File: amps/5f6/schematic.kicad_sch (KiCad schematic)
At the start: 69 parts, among them T3 2R sec

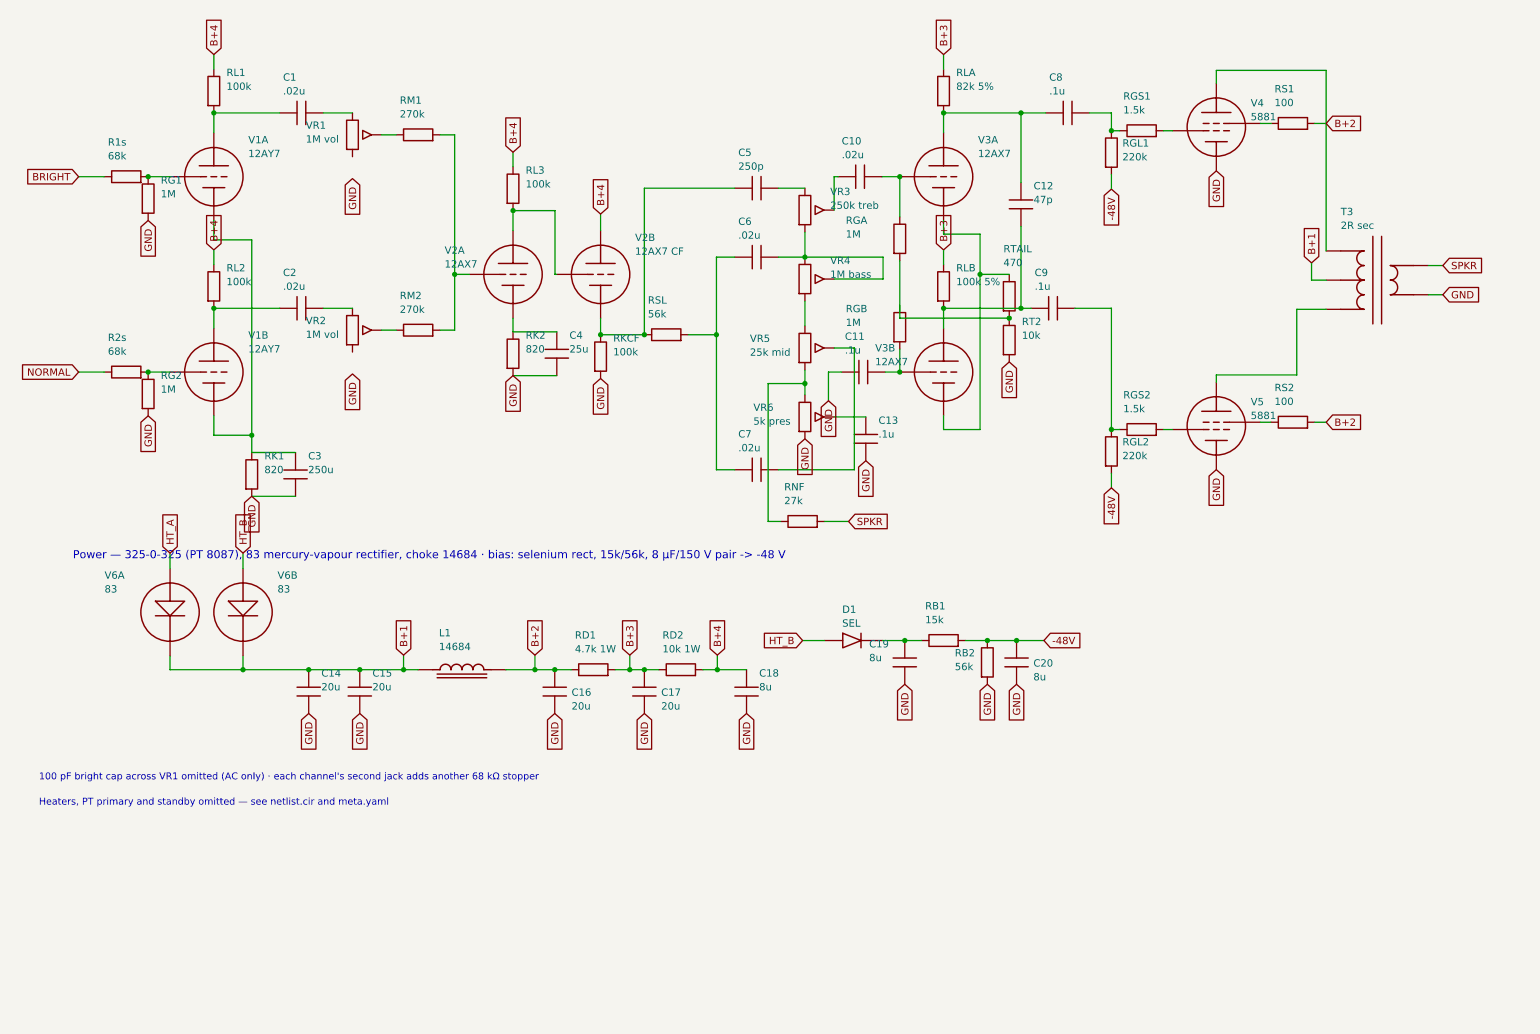
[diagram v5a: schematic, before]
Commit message: Fix: deterministic schematic ids and wires split at every join
- _u() is uuid5 over (amp id, emission order), so a regeneration of an
  unchanged script is byte-identical and a drift gate becomes possible
- write() splits wire segments at symbol pins, wire ends and junction dots,
  so the file connects exactly what the drawing shows under KiCad's
  endpoint-only semantics (270 pins were on a wire's interior; net
  partitions unchanged on all 38 sheets)
- all sheets regenerated; aa864-bassman title block was stale (draft) and
  now matches meta.yaml (verified)

Co-Authored-By: Claude Fable 5.1 <noreply@anthropic.com>
Claude-Session: https://claude.ai/code/session_01KBMfdh37HmCL2iWcBiL5J1
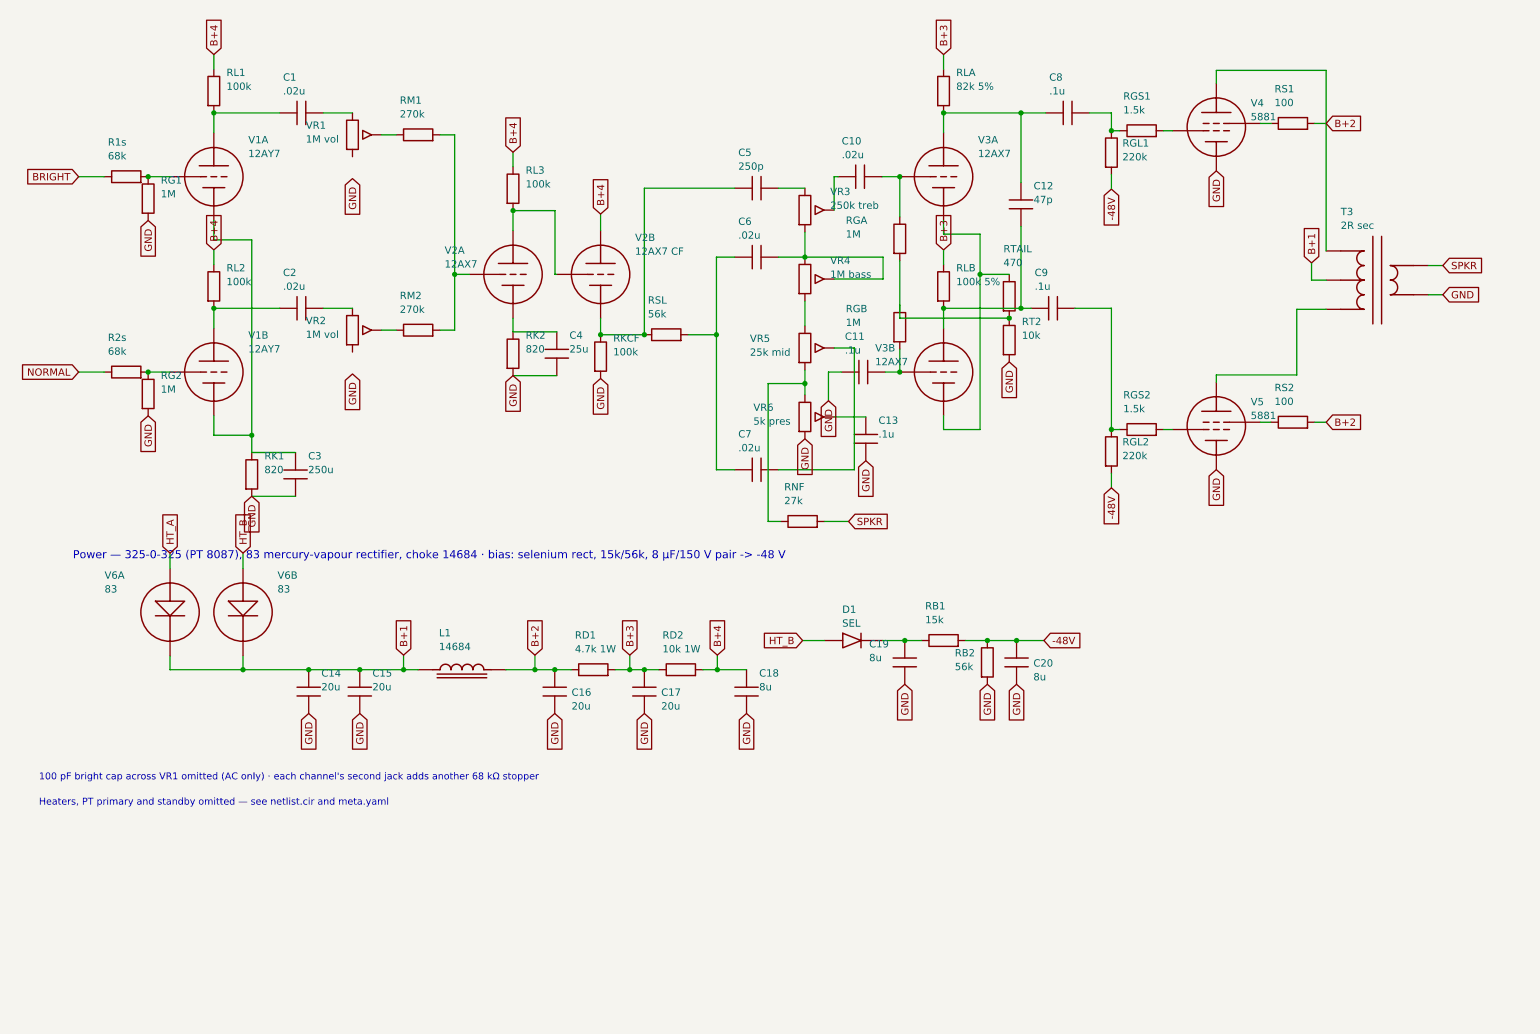
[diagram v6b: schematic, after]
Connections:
- net at RGA.2, RT2.1, RTAIL.2: now also RGB.1
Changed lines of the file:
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@@
   (wire (pts (xy 43.1388 83.278) (xy 49.7388 83.278))
     (stroke (width 0) (type default)))
-  (wire (pts (xy 49.7388 49.278) (xy 49.7388 86.278))
+  (wire (pts (xy 49.7388 49.278) (xy 49.7388 83.278))
+    (stroke (width 0) (type default)))
+  (wire (pts (xy 49.7388 83.278) (xy 49.7388 86.278))
     (stroke (width 0) (type default)))
   (junction (at 49.7388 83.278) (diameter 0) (color 0 0 0 0))
@@
     (property "Reference" "VR5" (at 136.437 66.448 0) (effects (font (size 1.27 1.27)) (justify left)))
     (property "Value" "25k mid" (at 136.437 68.848 0) (effects (font (size 1.27 1.27)) (justify left))))
-  (wire (pts (xy 146.009 71.898) (xy 146.009 76.278))
+  (wire (pts (xy 146.009 71.898) (xy 146.009 74.278))
+    (stroke (width 0) (type default)))
+  (wire (pts (xy 146.009 74.278) (xy 146.009 76.278))
     (stroke (width 0) (type default)))
   (junction (at 146.009 74.278) (diameter 0) (color 0 0 0 0))
@@
   (wire (pts (xy 170.139 82.278) (xy 176.489 82.278))
     (stroke (width 0) (type default)))
-  (wire (pts (xy 176.489 48.278) (xy 176.489 82.278))
+  (wire (pts (xy 176.489 48.278) (xy 176.489 55.278))
+    (stroke (width 0) (type default)))
+  (wire (pts (xy 176.489 55.278) (xy 176.489 82.278))
     (stroke (width 0) (type default)))
   (junction (at 176.489 55.278) (diameter 0) (color 0 0 0 0))
@@
     (property "Reference" "RGA" (at 153.119 45.888 0) (effects (font (size 1.27 1.27)) (justify left)))
     (property "Value" "1M" (at 153.119 48.288 0) (effects (font (size 1.27 1.27)) (justify left))))
-  (wire (pts (xy 162.519 52.898) (xy 162.519 62.898))
+  (wire (pts (xy 162.519 52.898) (xy 162.519 60.658))
+    (stroke (width 0) (type default)))
+  (wire (pts (xy 162.519 60.658) (xy 162.519 62.898))
     (stroke (width 0) (type default)))
   (wire (pts (xy 162.519 62.898) (xy 181.569 62.898))
@@
     (stroke (width 0) (type default)))
   (junction (at 183.609 61.178) (diameter 0) (color 0 0 0 0))
-  (wire (pts (xy 170.139 27.178) (xy 187.919 27.178))
+  (wire (pts (xy 170.139 27.178) (xy 183.609 27.178))
+    (stroke (width 0) (type default)))
+  (wire (pts (xy 183.609 27.178) (xy 187.919 27.178))
     (stroke (width 0) (type default)))
   (junction (at 170.139 27.178) (diameter 0) (color 0 0 0 0))
@@
   (global_label "GND" (shape input) (at 217.609 37.263 270)
     (effects (font (size 1.27 1.27)) (justify right)))
-  (wire (pts (xy 170.139 61.178) (xy 185.379 61.178))
+  (wire (pts (xy 170.139 61.178) (xy 183.609 61.178))
+    (stroke (width 0) (type default)))
+  (wire (pts (xy 183.609 61.178) (xy 185.379 61.178))
     (stroke (width 0) (type default)))
   (junction (at 170.139 61.178) (diameter 0) (color 0 0 0 0))
@@
   (wire (pts (xy 48.2188 121.678) (xy 48.2188 124.078))
     (stroke (width 0) (type default)))
-  (wire (pts (xy 35.5188 124.078) (xy 78.6988 124.078))
+  (wire (pts (xy 35.5188 124.078) (xy 48.2188 124.078))
+    (stroke (width 0) (type default)))
+  (wire (pts (xy 48.2188 124.078) (xy 59.6488 124.078))
+    (stroke (width 0) (type default)))
+  (wire (pts (xy 59.6488 124.078) (xy 68.5388 124.078))
+    (stroke (width 0) (type default)))
+  (wire (pts (xy 68.5388 124.078) (xy 76.1588 124.078))
+    (stroke (width 0) (type default)))
+  (wire (pts (xy 76.1588 124.078) (xy 78.6988 124.078))
     (stroke (width 0) (type default)))
   (junction (at 48.2188 124.078) (diameter 0) (color 0 0 0 0))
@@
     (property "Reference" "L1" (at 82.3188 117.678 0) (effects (font (size 1.27 1.27)) (justify left)))
     (property "Value" "14684" (at 82.3188 120.078 0) (effects (font (size 1.27 1.27)) (justify left))))
-  (wire (pts (xy 93.9388 124.078) (xy 105.369 124.078))
+  (wire (pts (xy 93.9388 124.078) (xy 99.0188 124.078))
+    (stroke (width 0) (type default)))
+  (wire (pts (xy 99.0188 124.078) (xy 102.469 124.078))
+    (stroke (width 0) (type default)))
+  (wire (pts (xy 102.469 124.078) (xy 105.369 124.078))
     (stroke (width 0) (type default)))
   (junction (at 99.0188 124.078) (diameter 0) (color 0 0 0 0))
@@
     (property "Reference" "RD1" (at 105.979 118.078 270) (effects (font (size 1.27 1.27)) (justify left)))
     (property "Value" "4.7k 1W" (at 105.979 120.478 270) (effects (font (size 1.27 1.27)) (justify left))))
-  (wire (pts (xy 112.989 124.078) (xy 120.609 124.078))
+  (wire (pts (xy 112.989 124.078) (xy 115.529 124.078))
+    (stroke (width 0) (type default)))
+  (wire (pts (xy 115.529 124.078) (xy 118.069 124.078))
+    (stroke (width 0) (type default)))
+  (wire (pts (xy 118.069 124.078) (xy 120.609 124.078))
     (stroke (width 0) (type default)))
   (junction (at 115.529 124.078) (diameter 0) (color 0 0 0 0))
@@
     (property "Reference" "RD2" (at 121.219 118.078 270) (effects (font (size 1.27 1.27)) (justify left)))
     (property "Value" "10k 1W" (at 121.219 120.478 270) (effects (font (size 1.27 1.27)) (justify left))))
-  (wire (pts (xy 128.229 124.078) (xy 135.849 124.078))
+  (wire (pts (xy 128.229 124.078) (xy 130.769 124.078))
+    (stroke (width 0) (type default)))
+  (wire (pts (xy 130.769 124.078) (xy 135.849 124.078))
     (stroke (width 0) (type default)))
   (junction (at 130.769 124.078) (diameter 0) (color 0 0 0 0))
@@
   (wire (pts (xy 163.389 118.998) (xy 166.329 118.998))
     (stroke (width 0) (type default)))
-  (wire (pts (xy 173.949 118.998) (xy 187.609 118.998))
+  (wire (pts (xy 173.949 118.998) (xy 177.759 118.998))
+    (stroke (width 0) (type default)))
+  (wire (pts (xy 177.759 118.998) (xy 182.839 118.998))
+    (stroke (width 0) (type default)))
+  (wire (pts (xy 182.839 118.998) (xy 187.609 118.998))
     (stroke (width 0) (type default)))
   (junction (at 177.759 118.998) (diameter 0) (color 0 0 0 0))

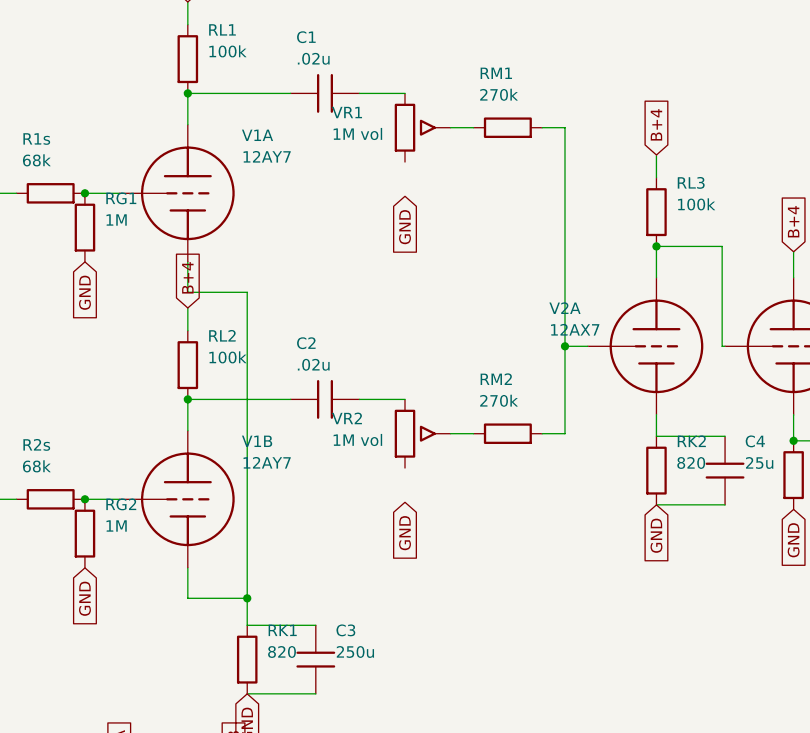
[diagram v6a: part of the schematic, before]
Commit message: Fix: schematic wiring on the tweed family, jtm45 and 6161
- pot cold lugs: s.gnd() sat 3.81 mm below cx:POT pin 3 on nine sheets
  (19 pins); every flag now lands on the lug
- retyped coordinates replaced by helper returns (5e5a OT pins alone freed
  nine pins; 5d3 V3 cathode, 5f10 RKB, 5e6a CBS, 5f2a dropper, grid leaks)
- shorts only verify_schematic_nets could see: 5e3 cathode bus through V4's
  screen pin (B+2 tied to the cathodes), C7 through RG6A, PI leak through
  RGPI, C8 on the cathode not the tail; 5f10 the same RGPI/C7 pair; 5e5a
  presence feed down the tube column; 5e6a RFB loop through RL3
- three dated waivers: two-terminal rheostat far lugs (5e6a VR5, 6161 VR3/VR4)

Co-Authored-By: Claude Fable 5.1 <noreply@anthropic.com>
Claude-Session: https://claude.ai/code/session_01KBMfdh37HmCL2iWcBiL5J1
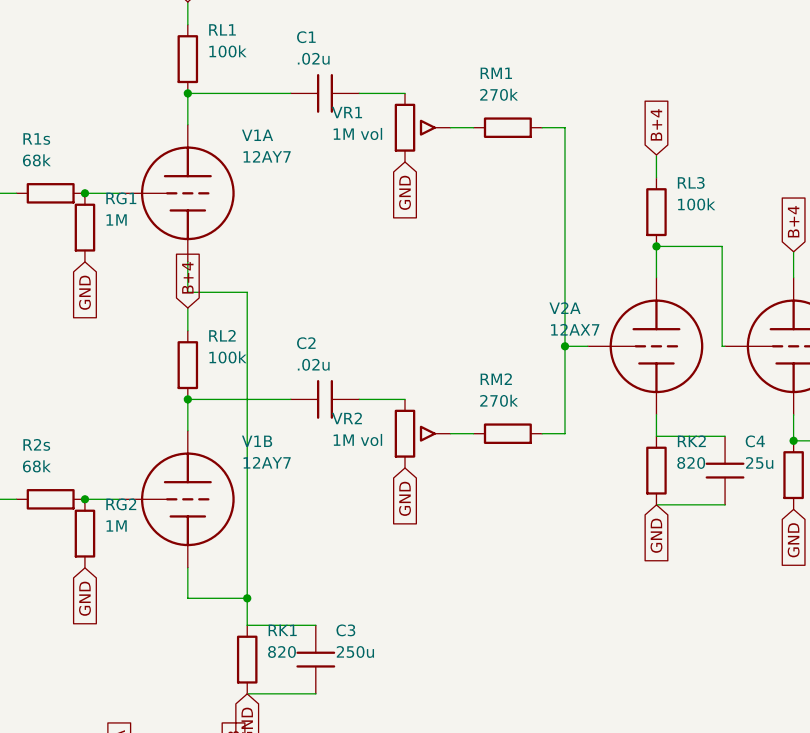
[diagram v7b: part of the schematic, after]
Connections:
- net GND: now also VR1.3, VR2.3
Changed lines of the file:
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@@
     (property "Reference" "VR1" (at 59.1476 29.348 0) (effects (font (size 1.27 1.27)) (justify left)))
     (property "Value" "1M vol" (at 59.1476 31.748 0) (effects (font (size 1.27 1.27)) (justify left))))
-  (global_label "GND" (shape input) (at 67.2688 38.608 270)
+  (global_label "GND" (shape input) (at 67.2688 34.798 270)
     (effects (font (size 1.27 1.27)) (justify right)))
   (wire (pts (xy 72.3488 30.988) (xy 74.8888 30.988))
@@
     (property "Reference" "VR2" (at 59.1476 63.348 0) (effects (font (size 1.27 1.27)) (justify left)))
     (property "Value" "1M vol" (at 59.1476 65.748 0) (effects (font (size 1.27 1.27)) (justify left))))
-  (global_label "GND" (shape input) (at 67.2688 72.608 270)
+  (global_label "GND" (shape input) (at 67.2688 68.798 270)
     (effects (font (size 1.27 1.27)) (justify right)))
   (wire (pts (xy 72.3488 64.988) (xy 74.8888 64.988))
